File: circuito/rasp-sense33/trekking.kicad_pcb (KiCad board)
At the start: 2 copper layers, 100 x 100 mm, 63 parts, among them J1 Raspberry Pi, J10 MOTOR, J11 OUT, J12 I2C0, J13 I2C0, J14 I2C0, J15 I2C0, J16 I2C0, J17 I2C0, J18 Module, J19 OUT, J2 ENCODER, J20 OUT, J21 INPUT, J22 INPUT, J23 UART, J3 ENCODER, J4 ENCODER, J5 ENCODER, J6 VIN, J7 VCC, J8 5VIN, J9 MOTOR, U1 RPI-PICO, U2 LM2596T-5, U3 ULN2803A

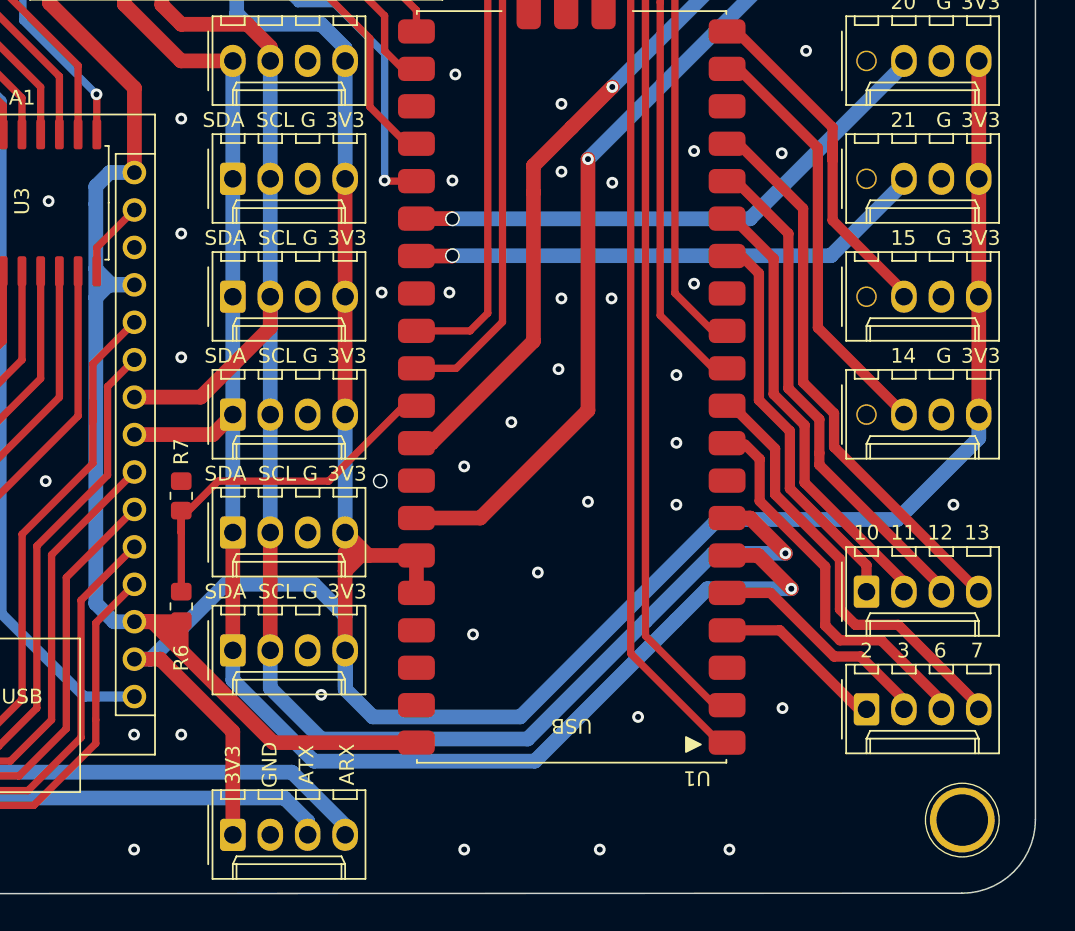
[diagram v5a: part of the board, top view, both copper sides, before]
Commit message: correção AREF PCI
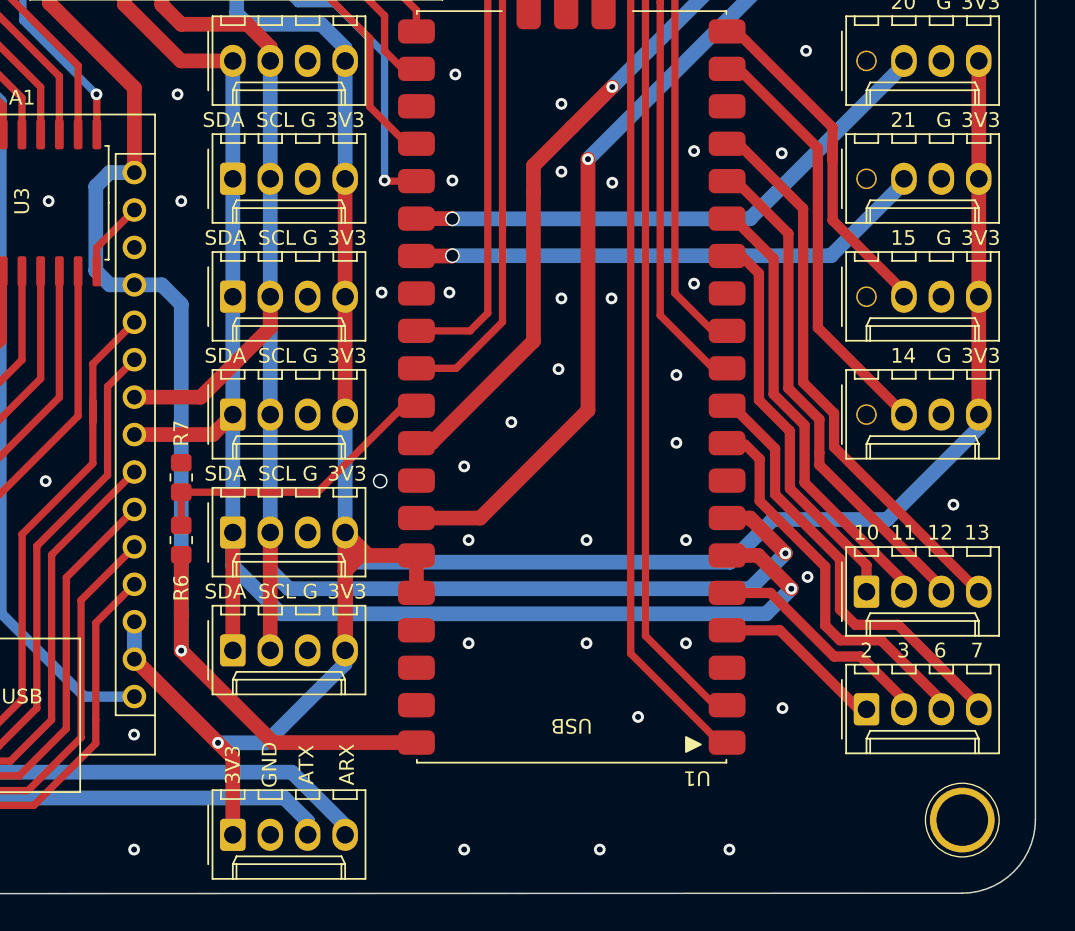
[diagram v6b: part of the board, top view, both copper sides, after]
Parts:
- J8: value 5VIN -> 5V
- moved R6 4.50 mm to (82.0, 131.0)
- moved R7 1.25 mm to (82.0, 126.8)
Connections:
- A1 pad 18: +5V -> +3V3
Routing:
- net +3V3: track 179.4 -> 172.1 mm, vias 0 -> 1
- net +5V: track 211.8 -> 206.2 mm, vias 0 -> 1
- net /SCL0: track 165.7 -> 160.6 mm
- net /ADC0: track 25.6 -> 20.6 mm
- net /SDA0: track 160.8 -> 156.4 mm
